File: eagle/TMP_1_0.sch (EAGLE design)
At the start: 15 parts, among them IC1 LM358N, U1 LM35, X1 Out~

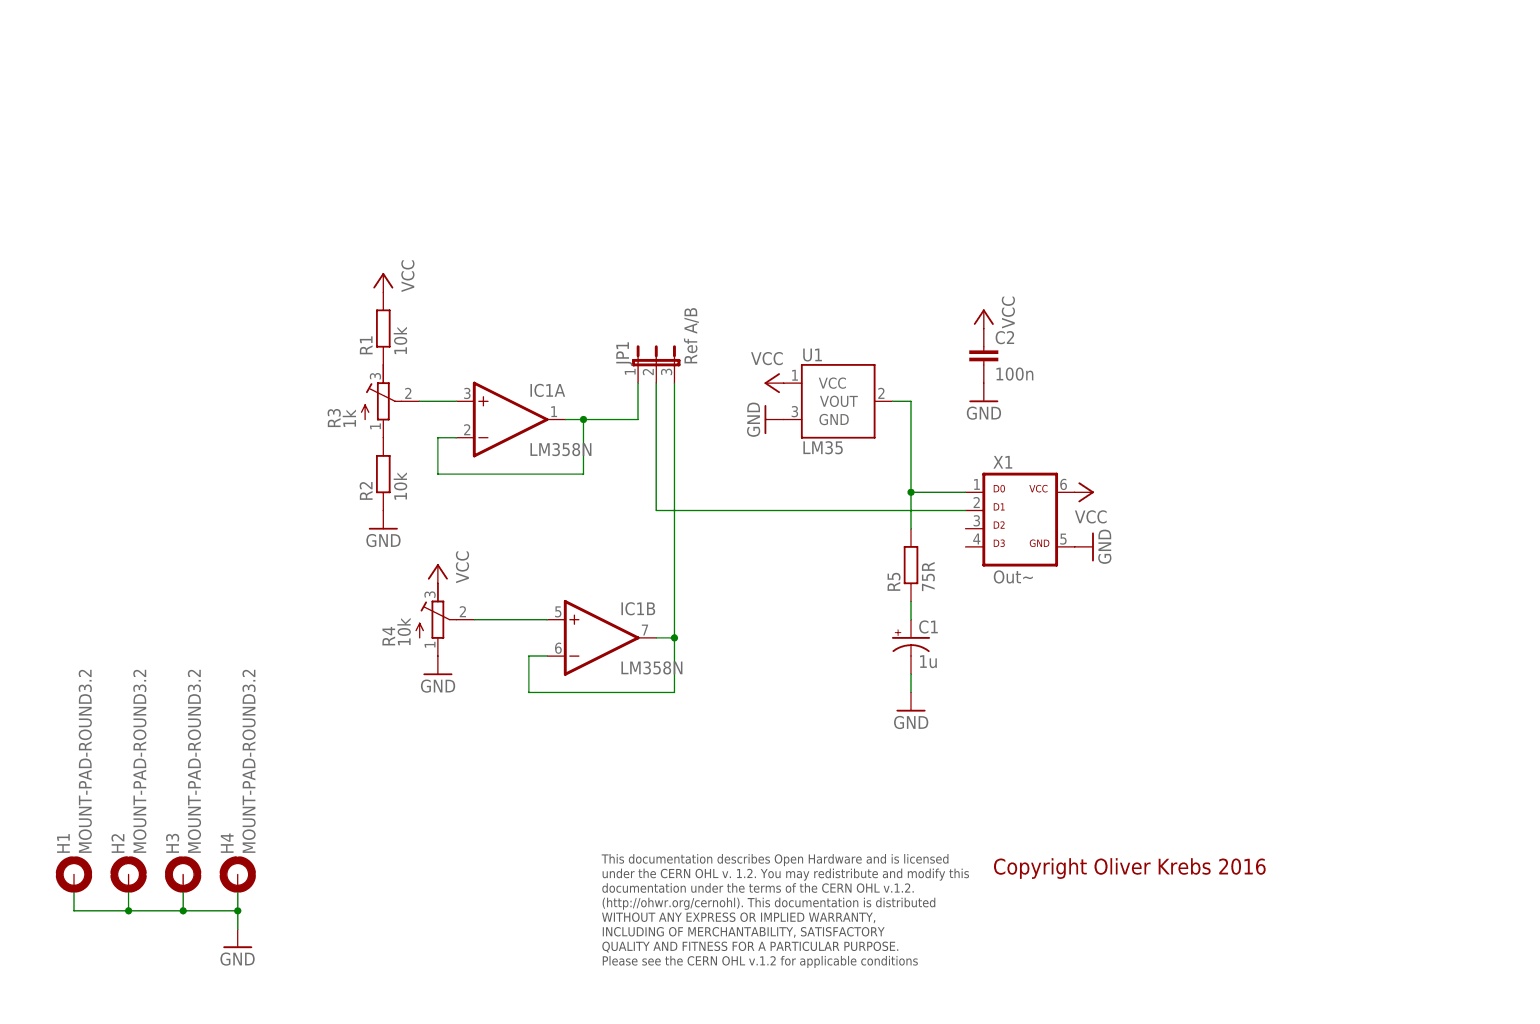
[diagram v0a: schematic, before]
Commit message: Add new tetra-Board and arduino files
Add AMP_1_0, AVC_1_0, D18_1_1, IOP_1_2, MIC_1_0, PIN_1_1, POT_1_0, PWA_1_0, PWR_1_0, RGF 2.0, SOC_2_0, VLT_1_0
Add mex_nano_shield_keyboard, mex_nano_shied_numbers

New arduino projects
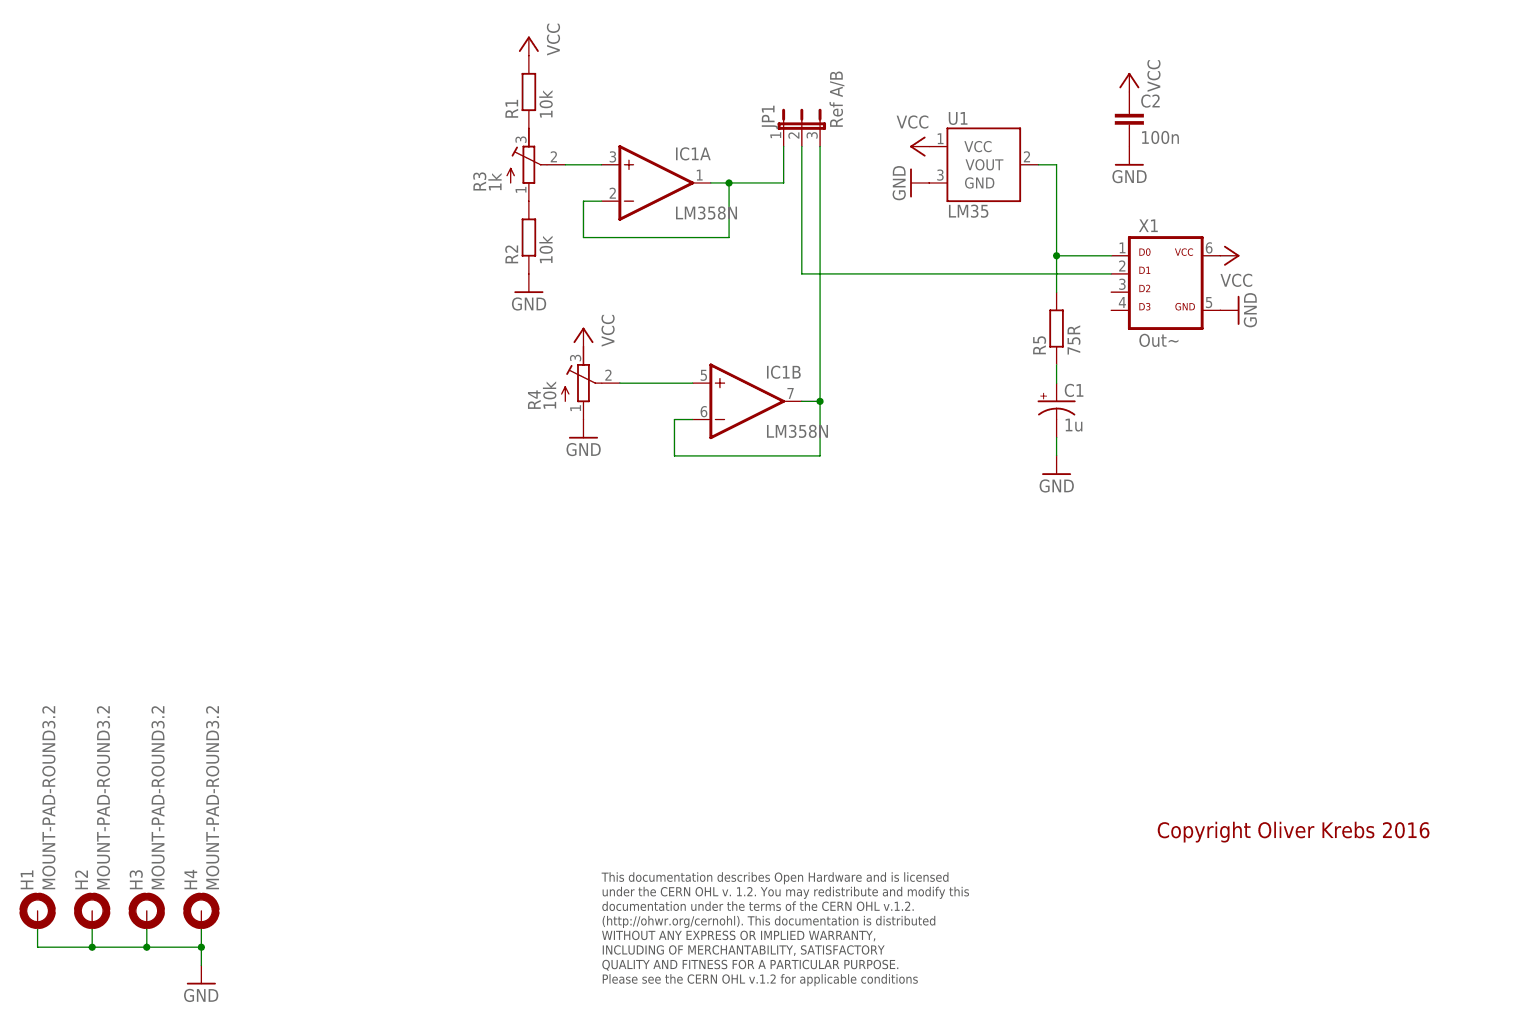
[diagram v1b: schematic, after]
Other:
- moved on the sheet: C1, C2, H1, H2, H3, H4, IC1A, IC1B, JP1, R1, R2, R3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
